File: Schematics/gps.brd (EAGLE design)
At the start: 53 x 57 mm, 23 parts, among them IC1 74HC14D, Q1 PE4259, Q2 MIC5365, U1 NEO-8Q, X1 REF_DC, X2 REF_AC

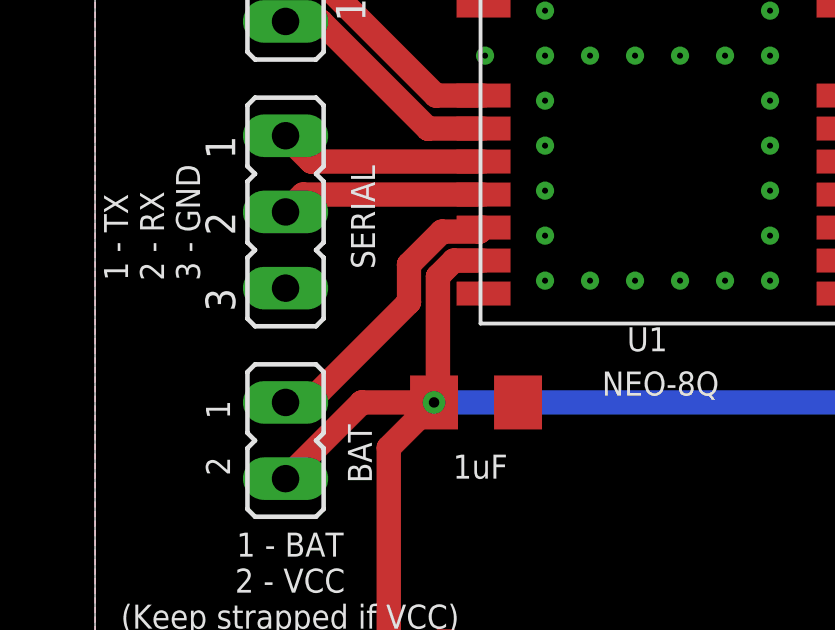
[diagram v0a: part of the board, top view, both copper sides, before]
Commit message: Straightened a Serial port Route
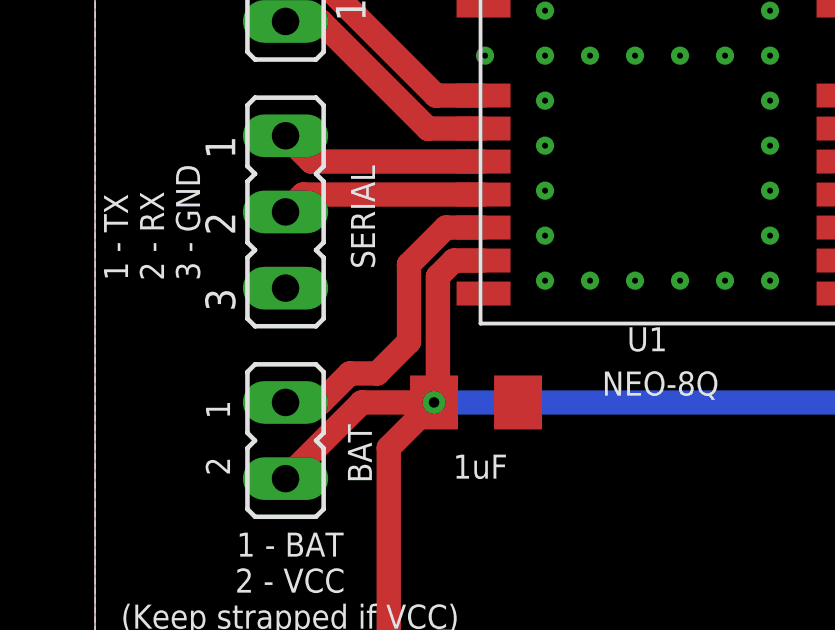
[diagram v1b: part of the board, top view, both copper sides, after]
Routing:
- net N$19: track 9.75 -> 10.5 mm
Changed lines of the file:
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@@
 <drawing>
 <settings>
-<setting alwaysvectorfont="yes"/>
+<setting alwaysvectorfont="no"/>
 <setting verticaltext="up"/>
 </settings>
@@
 <contactref element="U1" pad="22"/>
 <contactref element="JP6" pad="1"/>
-<wire x1="7.12" y1="27.94" x2="6.35" y2="27.94" width="0.8128" layer="1"/>
-<wire x1="12.95" y1="33.77" x2="12.8152" y2="33.6352" width="0.8128" layer="1"/>
-<wire x1="12.8152" y1="33.6352" x2="11.5599375" y2="33.6352" width="0.8128" layer="1"/>
-<wire x1="10.4648" y1="31.2848" x2="7.12" y2="27.94" width="0.8128" layer="1"/>
-<wire x1="11.5599375" y1="33.6352" x2="10.4648" y2="32.5400625" width="0.8128" layer="1"/>
-<wire x1="10.4648" y1="32.5400625" x2="10.4648" y2="31.2848" width="0.8128" layer="1"/>
+<wire x1="12.95" y1="33.77" x2="11.6947375" y2="33.77" width="0.8128" layer="1"/>
+<wire x1="11.6947375" y1="33.77" x2="10.4648" y2="32.5400625" width="0.8128" layer="1"/>
+<wire x1="9.4052" y1="28.9052" x2="8.4902" y2="28.9052" width="0.8128" layer="1"/>
+<wire x1="7.525" y1="27.94" x2="6.35" y2="27.94" width="0.8128" layer="1"/>
+<wire x1="8.4902" y1="28.9052" x2="7.525" y2="27.94" width="0.8128" layer="1"/>
+<wire x1="10.4648" y1="29.9648" x2="9.4052" y2="28.9052" width="0.8128" layer="1"/>
+<wire x1="10.4648" y1="32.5400625" x2="10.4648" y2="29.9648" width="0.8128" layer="1"/>
 </signal>
 <signal name="N$21">

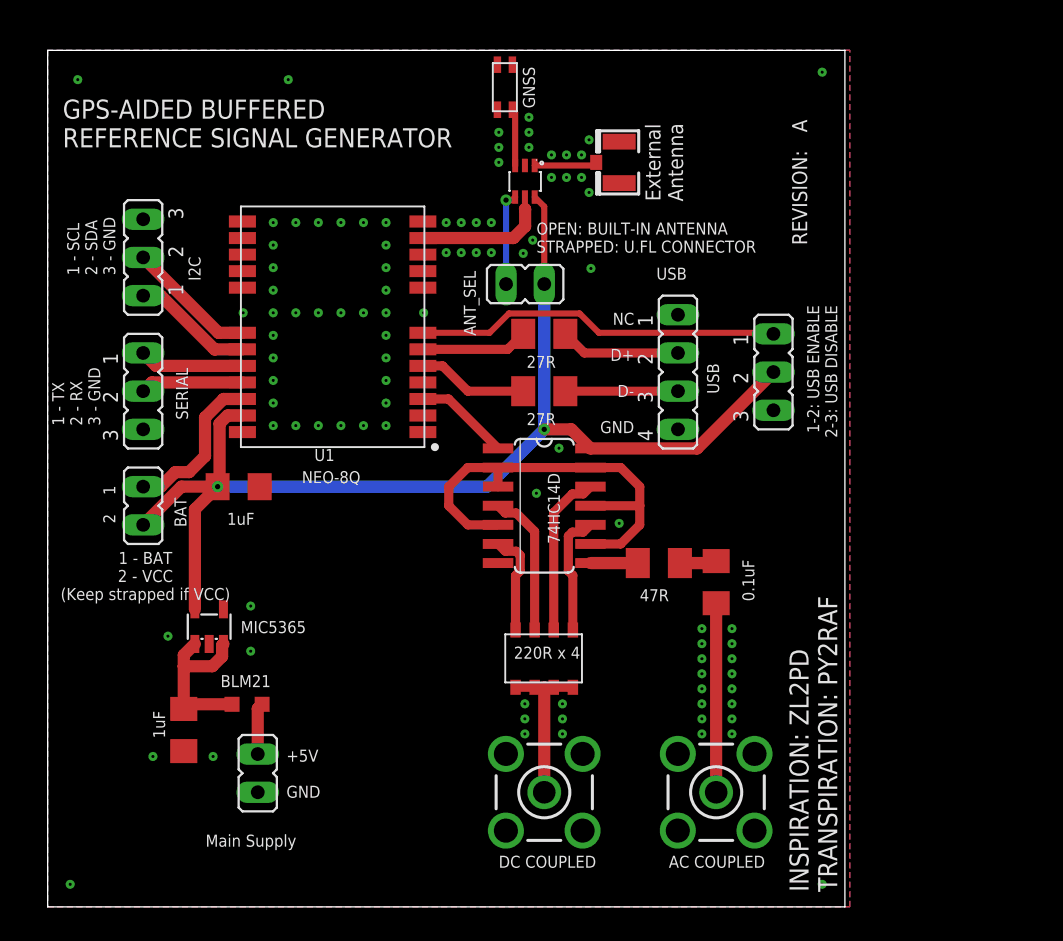
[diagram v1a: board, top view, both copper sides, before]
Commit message: New GPS version: Now feeding a Si5351
Test version.
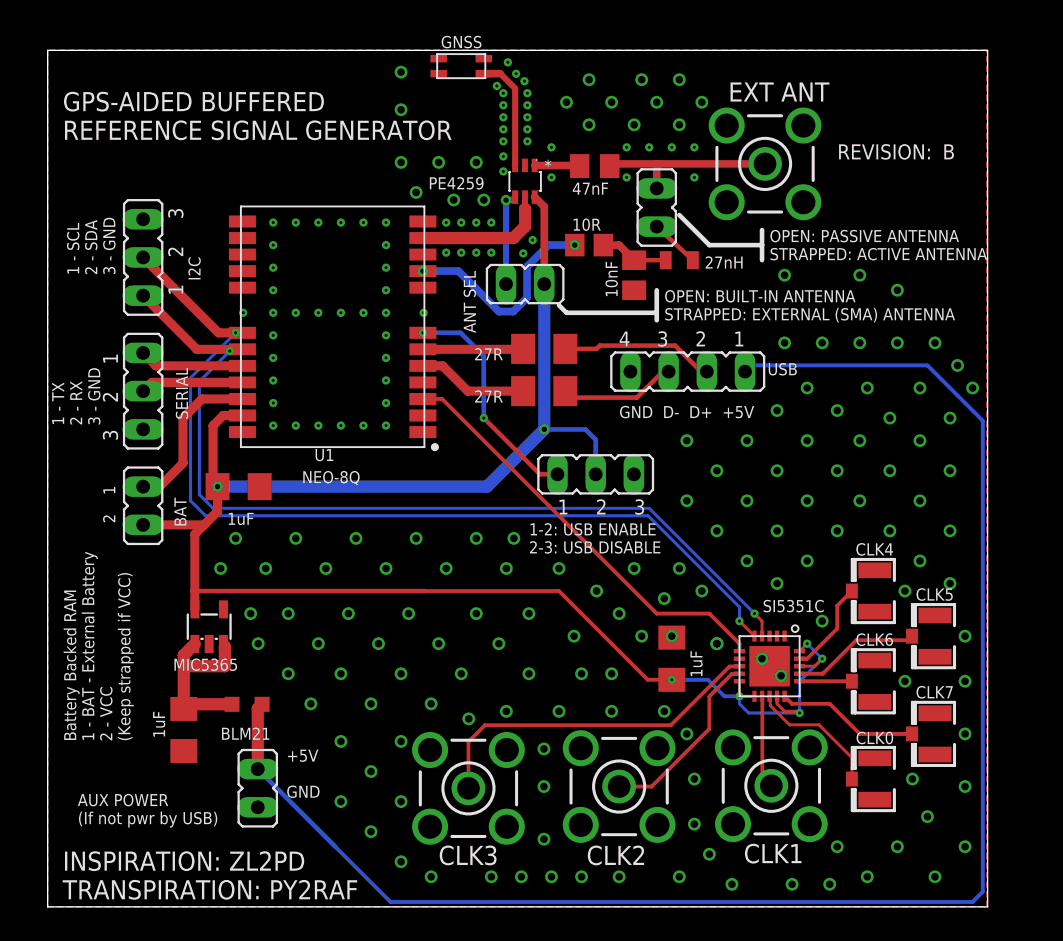
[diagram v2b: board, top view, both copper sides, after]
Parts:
- removed IC1: 74HC14D, 74xx-eu:SO14
- removed R2: 47R, rcl:M1206
- added C4: 1uF, rcl:C1206
- added C5: 47nF, rcl:C0805K
- added JP8: ACTIV, jumper:JP1
- added L2: 27nH, aarf:0805
- added Q3: SI5351C, aarf:QFN20
- added X10: CLK2, aarf:SMA-RF
- added X5: CLK4, adafruit:U.FL
- added X6: CLK5, adafruit:U.FL
- added X7: CLK6, adafruit:U.FL
- added X8: CLK7, adafruit:U.FL
- added X9: CLK0, adafruit:U.FL
- C1: value 0.1uF -> 10nF; device rcl:C1206 -> rcl:C0805K
- JP5: value ANT_SEL -> ANT SEL
- R1: value (none) -> 10R; device aarf:1206X4 -> rcl:R0805
- X1: value REF_DC -> CLK3
- X2: value REF_AC -> CLK1
- X4: value (none) -> EXT ANT; device adafruit:U.FL -> aarf:SMA-RF
- moved R1 27.7 mm to (36.0, 44.0), turned to 0 degrees
- moved C1 21.1 mm to (39.0, 42.0), turned to 270 degrees
- moved JP4 13.6 mm to (36.4, 28.8), turned to 0 degrees
- moved X4 9.70 mm to (47.7, 49.4), turned to 0 degrees
- moved X1 5.05 mm to (28.0, 7.88), turned to 180 degrees
- moved X2 3.70 mm to (48.1, 8.05), turned to 270 degrees
- moved X3 3.35 mm to (27.5, 56.0), turned to 180 degrees
- moved JP7 1.00 mm to (14.0, 7.89)
- moved R4 1.00 mm to (33.0, 37.1)
- moved JP3 0.65 mm to (42.6, 35.6), turned to 180 degrees
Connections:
- removed net N$4: IC1.10, R1.P$1
- new net N$28: JP3.1, JP7.2, L1.1
- new net N$29: Q3.15, X8.3
- new net N$30: Q3.13, X9.3
- new net N$31: Q3.8, X1.1
- net GNDA: now also C1.2, C4.2, Q3.21, Q3.7, X10.2, X10.3, X10.4, X10.5, X3.P$1, X4.3, X4.4, X4.5, X5.1, X5.2, X6.1, X6.2, X7.1, X7.2, X8.1, X8.2, X9.1, X9.2; no longer IC1.7, X3.P$2, X4.1
- net N$1: now also Q3.6, U1.3; no longer IC1.11, IC1.13, IC1.2, IC1.3, IC1.5, IC1.9
- net N$11: now also JP8.1, L2.P$1; no longer C1.1, X2.1
- net N$15: now also Q3.5
- net N$16: now also Q3.4
- net N$2: now also Q3.12, X2.1; no longer IC1.4, R1.P$3
- net N$21: now also Q3.19, X5.3; no longer R1.P$5, R1.P$6, R1.P$7, R1.P$8, X1.1
- net N$22: now also C4.1, Q3.10, Q3.11, Q3.14, Q3.18, Q3.20; no longer IC1.14
- net N$25: now also Q3.17, X6.3; no longer JP7.2, L1.1
- net N$26: now also X3.P$2; no longer X3.P$1
- net N$27: now also Q3.16, X7.3; no longer Q1.1, X4.3
- net N$3: now also Q3.9, X10.1; no longer IC1.12, R1.P$2
- net N$5: now also C5.2, JP8.2, X4.1; no longer IC1.6, R1.P$4
- net N$6: now also C5.1, Q1.1; no longer IC1.1, U1.3
- net N$7: now also R1.1, U1.9; no longer IC1.8, R2.1
- net N$8: now also C1.1, L2.P$2, R1.2; no longer C1.2, R2.2
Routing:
- net N$28: track 0.00 -> 105.4 mm
- net N$15: track 8.68 -> 62.9 mm, vias 0 -> 2
- net N$16: track 8.08 -> 60.4 mm, vias 0 -> 2
- net N$22: track 78.0 -> 120.9 mm, vias 2 -> 7
- net N$31: track 0.00 -> 23.2 mm
- net N$7: track 3.15 -> 14.3 mm, vias 0 -> 2
- net N$29: track 0.00 -> 9.51 mm
- net N$11: track 12.6 -> 3.28 mm
- net N$12: track 24.4 -> 15.3 mm, vias 0 -> 2
- net N$30: track 0.00 -> 8.95 mm
- net N$4: track 8.15 -> 0.00 mm
- net N$5: track 6.88 -> 12.0 mm
- net N$25: track 3.43 -> 8.51 mm
- net N$21: track 10.6 -> 6.23 mm
- net N$26: track 3.78 -> 7.61 mm
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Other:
- board size 53 x 57 mm -> 62.5 x 57 mm
- board text added: "AUX POWER (If not pwr by USB)"
- board text added: "Battery Backed RAM 1 - BAT - External Battery 2 - VCC (Keep strapped if VCC)"
- board text added: "GND D- D+ +5V"
- board text added: "OPEN: BUILT-IN ANTENNA STRAPPED: EXTERNAL (SMA) ANTENNA"
- board text added: "OPEN: PASSIVE ANTENNA STRAPPED: ACTIVE ANTENNA"
- board text removed: "1 - BAT 2 - VCC (Keep strapped if VCC)"
- board text removed: "220R x 4"
- board text removed: "AC COUPLED"
- board text removed: "DC COUPLED"
- board text removed: "External Antenna"
- board text removed: "Main Supply"
- board text removed: "NC D+ D- GND"
- board text removed: "OPEN: BUILT-IN ANTENNA STRAPPED: U.FL CONNECTOR"
- board text removed: "USB"

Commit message: Rev. B: Pull-up in I2C, new GPS Clock port
* Implemented I²C pull-up resistors (required by datasheet)
* Added a U.FL connector in the GPS clock port that drives the 5351 in
  for test / troubleshoot
* Added schematic, gerber, pictures
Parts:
- added R2, R5: 1kR, rcl:R1206
- added X11: GPS CLK, adafruit:U.FL
- JP4: value USB_EN -> USB EN
- X3: value (none) -> GNSS
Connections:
- net GNDA: now also X11.1, X11.2
- net N$1: now also X11.3
- net N$15: now also R2.2
- net N$16: now also R5.2
- net N$22: now also R2.1, R5.1
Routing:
- net N$22: track 120.9 -> 123.9 mm
- net N$15: track 62.9 -> 64.4 mm, vias 2 -> 3
- net N$16: track 60.4 -> 61.4 mm, vias 2 -> 3
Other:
- board text added: "GPS-AIDED REFERENCE SIGNAL GENERATOR"
- board text removed: "GPS-AIDED BUFFERED REFERENCE SIGNAL GENERATOR"

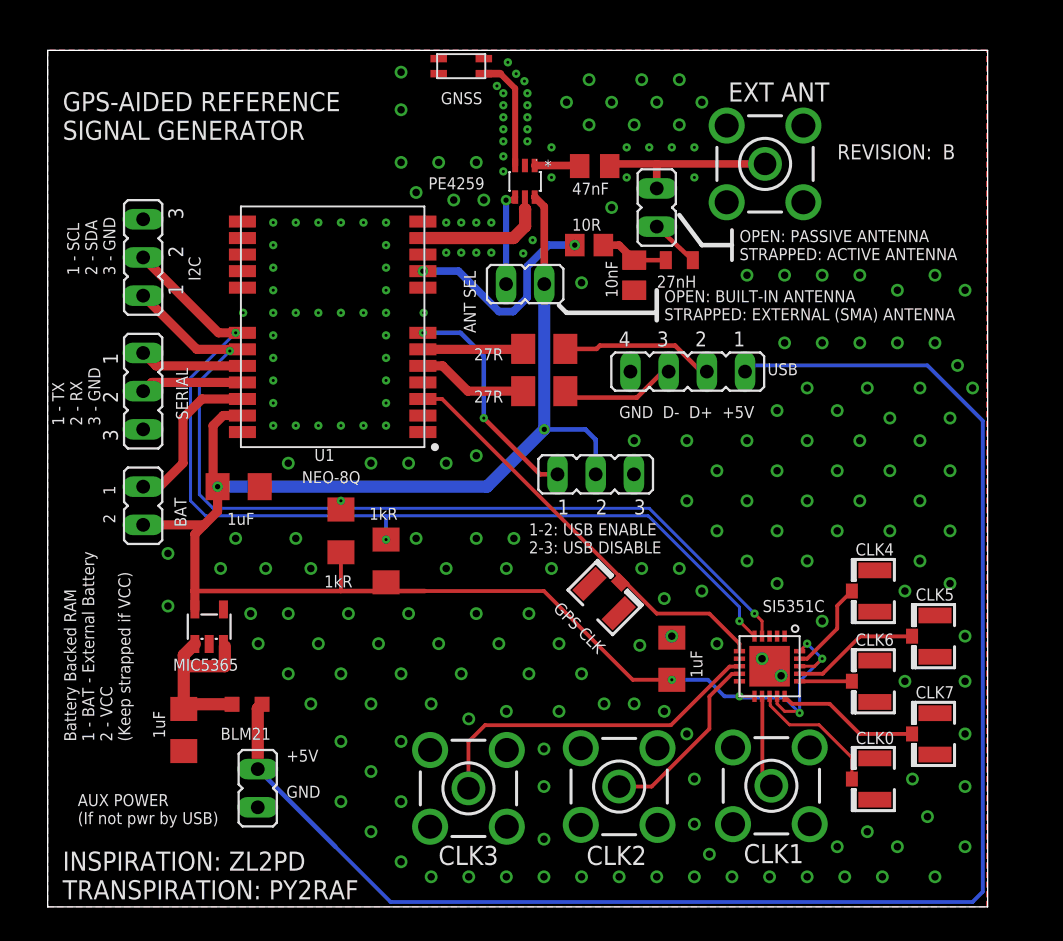
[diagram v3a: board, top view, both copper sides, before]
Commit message: GPS board: I2C changes
* Separated to two independent I2C ports, one for the uBlox, other for
  the 5351
* Minor re-routing
* Updated BOM, schematics and stuff
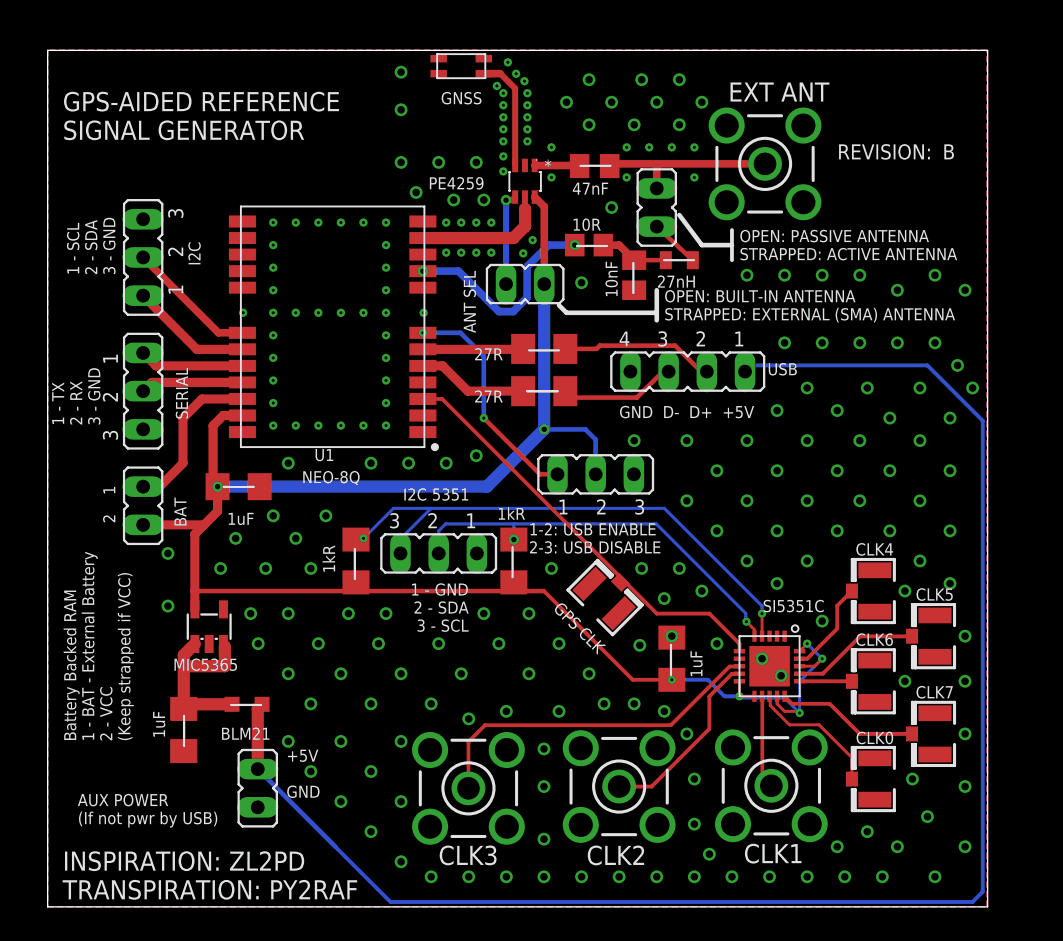
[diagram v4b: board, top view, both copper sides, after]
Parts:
- added JP9: ACTIV, jumper:JP1
- C1: value 10nF -> 1uF; device rcl:C0805K -> rcl:C1206
- C3: value 1uF -> 47nF; device rcl:C1206 -> rcl:C0805K
- C5: value 47nF -> 10nF
- JP1: value SERIAL -> +5V; device jumper:JP2 -> jumper:JP1
- JP3: value USB -> SERIAL; device jumper:JP4 -> jumper:JP2
- JP4: value USB EN -> BAT; device jumper:JP2 -> jumper:JP1
- JP5: value ANT SEL -> USB EN; device jumper:JP1 -> jumper:JP2
- JP6: value BAT -> ANT SEL
- JP7: value +5V -> USB; device jumper:JP1 -> jumper:JP4
- JP8: value ACTIV -> I2C 5351; device jumper:JP1 -> jumper:JP2
- Q1: value PE4259 -> MIC5365; device aarf:SC-70 -> aarf:SOT23-5L
- Q2: value MIC5365 -> PE4259; device aarf:SOT23-5L -> aarf:SC-70
- R1: value 10R -> 27R; device rcl:R0805 -> rcl:M1206
- R2: value 1kR -> 27R; device rcl:R1206 -> rcl:M1206
- R3, R4: value 27R -> 1kR; device rcl:M1206 -> rcl:R1206
- R5: value 1kR -> 10R; device rcl:R1206 -> rcl:R0805
- X1: value CLK3 -> GPS CLK; device aarf:SMA-RF -> adafruit:U.FL
- X10: value CLK2 -> CLK7; device aarf:SMA-RF -> adafruit:U.FL
- X11: value GPS CLK -> CLK1; device adafruit:U.FL -> aarf:SMA-RF
- X2: value CLK1 -> GNSS; device aarf:SMA-RF -> aarf:MOLEX-GNSS
- X3: value GNSS -> CLK2; device aarf:MOLEX-GNSS -> aarf:SMA-RF
- X4: value EXT ANT -> CLK3
- X5: value CLK4 -> EXT ANT; device adafruit:U.FL -> aarf:SMA-RF
- X6: value CLK5 -> CLK0
- X7: value CLK6 -> CLK4
- X8: value CLK7 -> CLK6
- X9: value CLK0 -> CLK5
- moved X2 52.2 mm to (27.5, 56.0), turned to 180 degrees
- moved X3 49.1 mm to (38.0, 8.00), turned to 0 degrees
- moved C3 46.4 mm to (36.4, 49.3), turned to 0 degrees
- moved X4 46.0 mm to (28.0, 7.88), turned to 180 degrees
- moved C1 42.6 mm to (9.05, 11.8)
- moved JP7 39.8 mm to (42.6, 35.6), turned to 180 degrees
- moved Q1 36.3 mm to (10.7, 18.6), turned to 0 degrees
- moved Q2 36.3 mm to (31.8, 48.3), turned to 180 degrees
- moved JP3 36.2 mm to (6.35, 34.3), turned to 270 degrees
- moved JP4 30.2 mm to (6.35, 26.7), turned to 180 degrees
- moved JP6 29.4 mm to (31.8, 41.4), turned to 90 degrees
- moved X5 29.3 mm to (47.7, 49.4), turned to 0 degrees
- moved JP1 27.5 mm to (14.0, 7.89), turned to 0 degrees
- moved JP8 27.2 mm to (26.0, 23.5), turned to 180 degrees
- moved R5 25.2 mm to (36.0, 44.0), turned to 0 degrees
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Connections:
- new net N$32: JP8.2, Q3.5, R3.2
- new net N$4: JP8.3, Q3.4, R4.2
- net GNDA: now also C5.2, JP1.1, JP3.3, JP5.3, JP7.4, JP8.1, X1.1, X10.1, X11.3, X11.4, X11.5, X2.P$1, X2.P$3, X2.P$4, X3.2, X3.3, X3.4, X3.5, X5.3, X5.4, X5.5; no longer C3.2, JP1.3, JP3.4, JP4.3, JP7.1, X1.3, X1.4, X1.5, X10.3, X10.4, X10.5, X11.1, X2.2, X2.3, X2.4, X2.5, X3.P$1, X3.P$3, X3.P$4, X5.1
- net N$1: now also X1.3; no longer X11.3
- net N$10: now also R2.2; no longer R4.2
- net N$11: now also JP9.1; no longer JP8.1
- net N$12: now also JP5.1; no longer JP4.1
- net N$13: now also JP7.3, R1.1; no longer JP3.3, R3.1
- net N$14: now also JP7.2, R2.1; no longer JP3.2, R4.1
- net N$15: no longer Q3.5, R2.2
- net N$16: no longer Q3.4, R5.2
- net N$17: now also JP3.2; no longer JP1.2
- net N$18: now also JP3.1; no longer JP1.1
- net N$19: now also JP4.1; no longer JP6.1
- net N$2: now also X11.1; no longer X2.1
- net N$20: now also JP6.2, Q2.4; no longer JP5.2, Q1.4
- net N$21: now also X7.3; no longer X5.3
- net N$22: now also JP5.2, JP6.1, Q1.5, Q2.6, R3.1, R4.1; no longer JP5.1, JP6.2, Q1.6, Q2.5, R2.1, R5.1
- net N$23: now also Q2.5; no longer Q1.5
- net N$24: now also C1.1, Q1.1, Q1.3; no longer C3.1, Q2.1, Q2.3
- net N$25: now also X9.3; no longer X6.3
- net N$26: now also Q2.3, X2.P$2; no longer Q1.3, X3.P$2
- net N$27: now also X8.3; no longer X7.3
- net N$28: now also JP1.2, JP7.1; no longer JP3.1, JP7.2
- net N$29: now also X10.3; no longer X8.3
- net N$3: now also X3.1; no longer X10.1
- net N$30: now also X6.3; no longer X9.3
- net N$31: now also X4.1; no longer X1.1
- net N$5: now also C3.2, JP9.2, X5.1; no longer C5.2, JP8.2, X4.1
- net N$6: now also C3.1, Q2.1; no longer C5.1, Q1.1
- net N$7: now also R5.1; no longer R1.1
- net N$8: now also C5.1, R5.2; no longer C1.1, R1.2
- net N$9: now also R1.2; no longer R3.2
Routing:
- net N$15: track 64.4 -> 8.68 mm, vias 3 -> 0
- net N$16: track 61.4 -> 8.08 mm, vias 3 -> 0
- net N$4: track 0.00 -> 36.4 mm, vias 0 -> 2
- net N$32: track 0.00 -> 27.4 mm, vias 0 -> 2
- net N$22: track 123.9 -> 121.9 mm
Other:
- board text added: "1 - GND 2 - SDA 3 - SCL"

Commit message: Sync-up
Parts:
- L2: device aarf:0805 -> aarf:0603
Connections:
- net N$11: now also L2.1; no longer L2.P$1
- net N$8: now also L2.2; no longer L2.P$2
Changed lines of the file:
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@@
 <attribute name="VALUE" x="34.873" y="47.354" size="0.8" layer="25" font="vector" ratio="15"/>
 </element>
-<element name="L2" library="aarf" package="0805" value="27nH" x="42" y="43" smashed="yes" rot="R180">
+<element name="L2" library="aarf" package="0603" value="27nH" x="42" y="43" smashed="yes" rot="R180">
 <attribute name="VALUE" x="43.13" y="41.97" size="0.8" layer="25" font="vector" ratio="15" rot="R180"/>
 </element>
@@
 <wire x1="36.95" y1="44" x2="38" y2="44" width="0.508" layer="1"/>
 <wire x1="38" y1="44" x2="39" y2="43" width="0.508" layer="1"/>
-<contactref element="L2" pad="P$2"/>
-<wire x1="41.1" y1="43" x2="39" y2="43" width="0.3048" layer="1"/>
+<contactref element="L2" pad="2"/>
+<wire x1="41.15" y1="43" x2="39" y2="43" width="0.3048" layer="1"/>
 </signal>
 <signal name="N$11">
-<contactref element="L2" pad="P$1"/>
+<contactref element="L2" pad="1"/>
 <contactref element="JP9" pad="1"/>
-<wire x1="40.5" y1="45.23" x2="42.9" y2="43" width="0.3048" layer="1"/>
+<wire x1="40.5" y1="45.23" x2="42.85" y2="43" width="0.3048" layer="1"/>
 </signal>
 <signal name="N$21">
